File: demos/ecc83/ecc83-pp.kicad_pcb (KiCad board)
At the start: 2 copper layers, 15 parts, among them P1 IN, P2 OUT, P3 POWER, P4 CONN_2, U1 ECC81_83

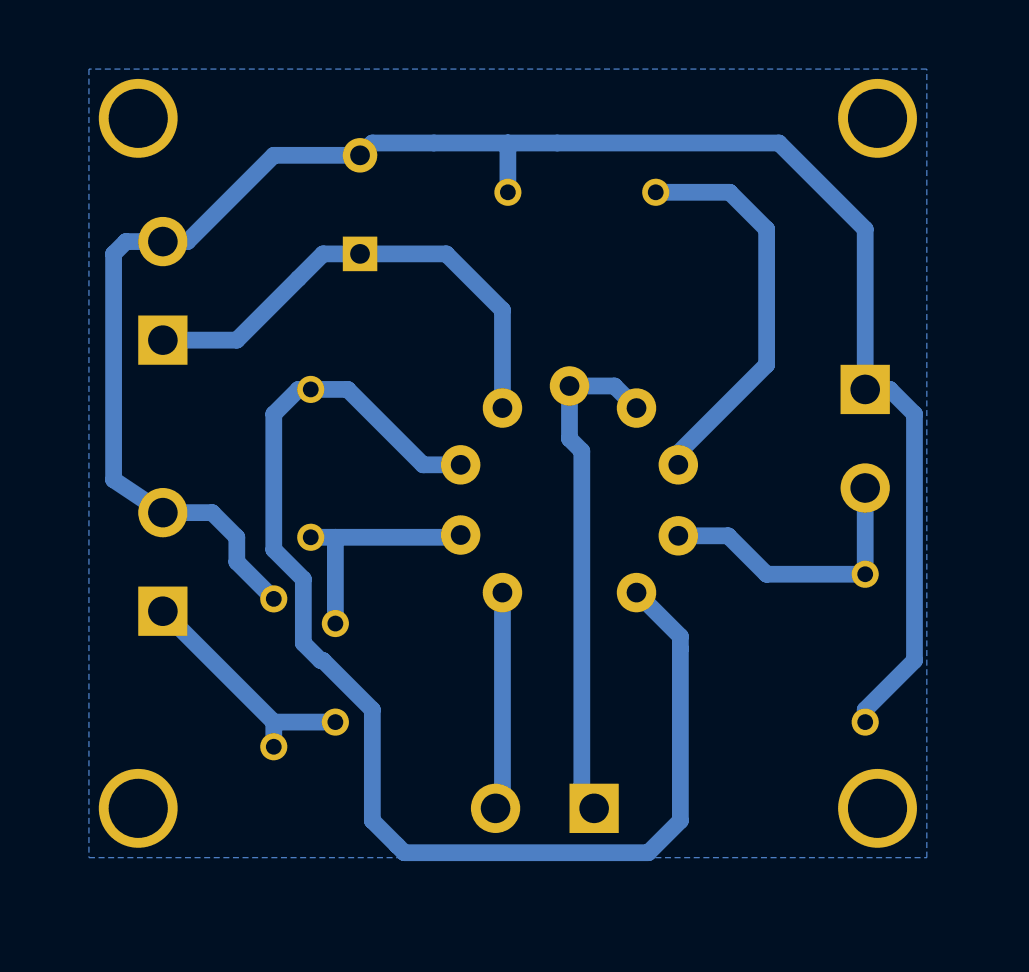
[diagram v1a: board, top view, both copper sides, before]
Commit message: Update old demo board files. Minor code cleaning.
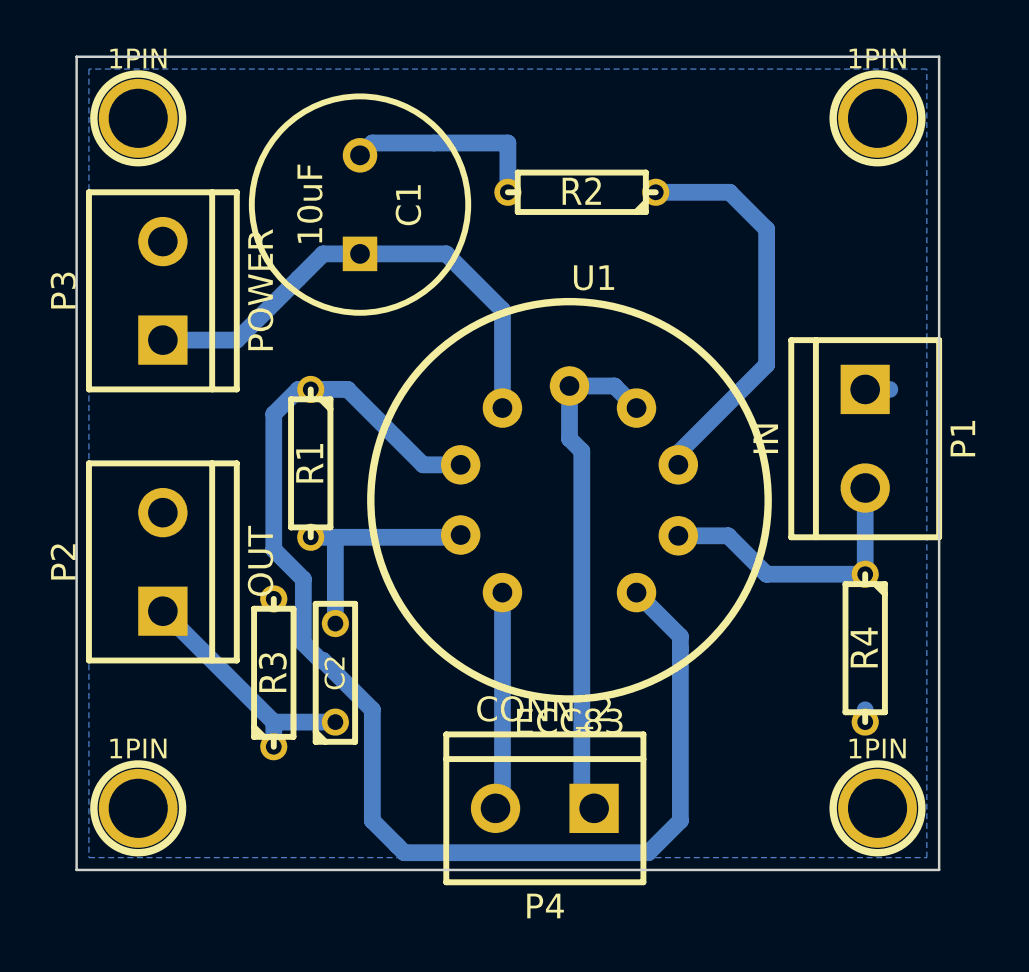
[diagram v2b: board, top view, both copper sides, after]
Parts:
- U1: value ECC81_83 -> ECC83
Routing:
- net GND: track 96.7 -> 12.3 mm
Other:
- board outline added: 44.5 x 41.9 mm

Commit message: Update ecc83 demo. default KISYS3DMOD definition on Linux: add /usr/local/kicad/share/kicad/module/package3d test to find a suitable value.
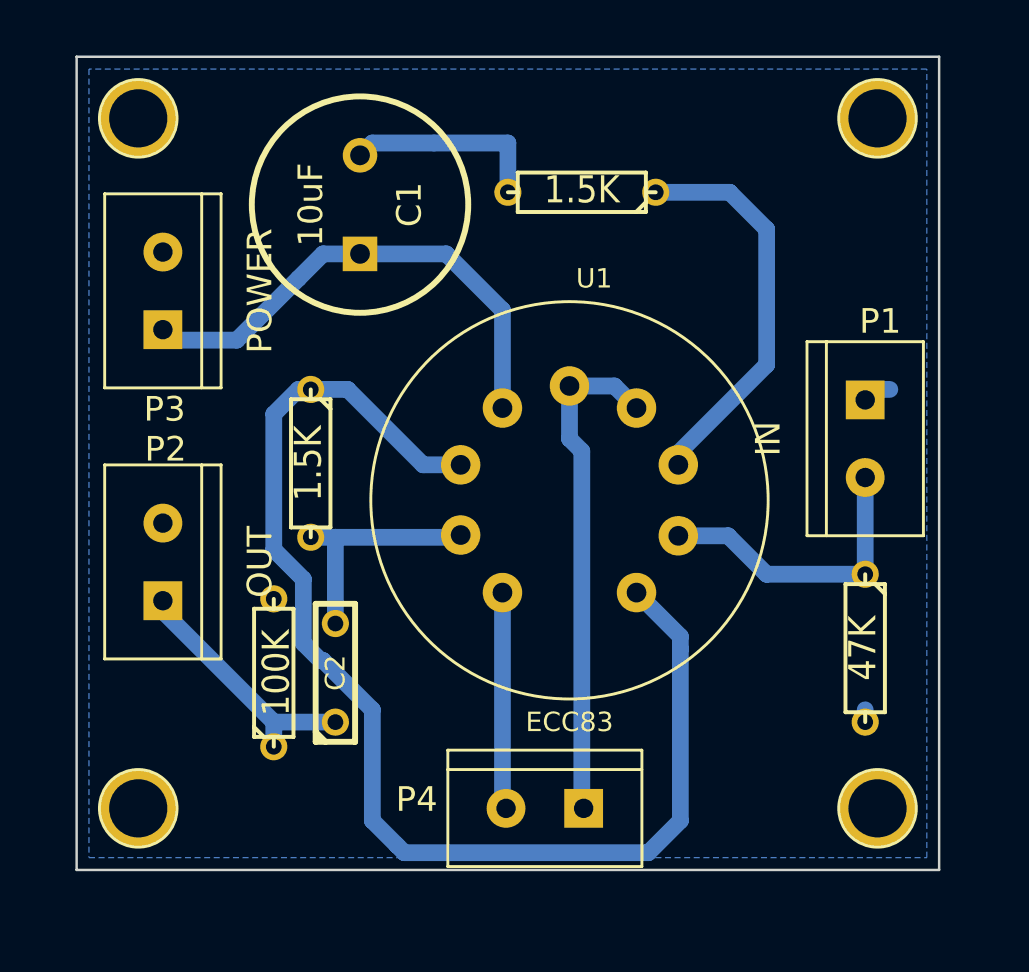
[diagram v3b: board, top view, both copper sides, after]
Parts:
- removed 1PIN (x4): P***, 1pin
- added P5: CONN_1, connect:1pin, F.Cu at (127.0, 94.0)
- added P6: CONN_1, connect:1pin, F.Cu at (165.1, 94.0)
- added P7: CONN_1, connect:1pin, F.Cu at (165.1, 129.5)
- added P8: CONN_1, connect:1pin, F.Cu at (127.0, 129.5)
- C1: footprint C2V10 -> discret:C2V10
- C2: footprint C2 -> discret:C2
- P1, P2, P3, P4: footprint bornier2 -> connect:bornier2
- R1, R2, R3, R4: footprint R3 -> discret:R3
- U1: footprint ECC-83-1 -> Valves:VALVE-ECC-83-1
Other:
- rule pad_to_mask_clearance: 0.254 -> 0.1
